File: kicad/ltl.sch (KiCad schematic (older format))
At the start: 17 parts, among them J1 CONN_01X03, J2 BARREL_JACK, SW1 SW_DIP_x02, SW2 SW_DIP_x02, U1 ESP-12E, U2 DS18B20

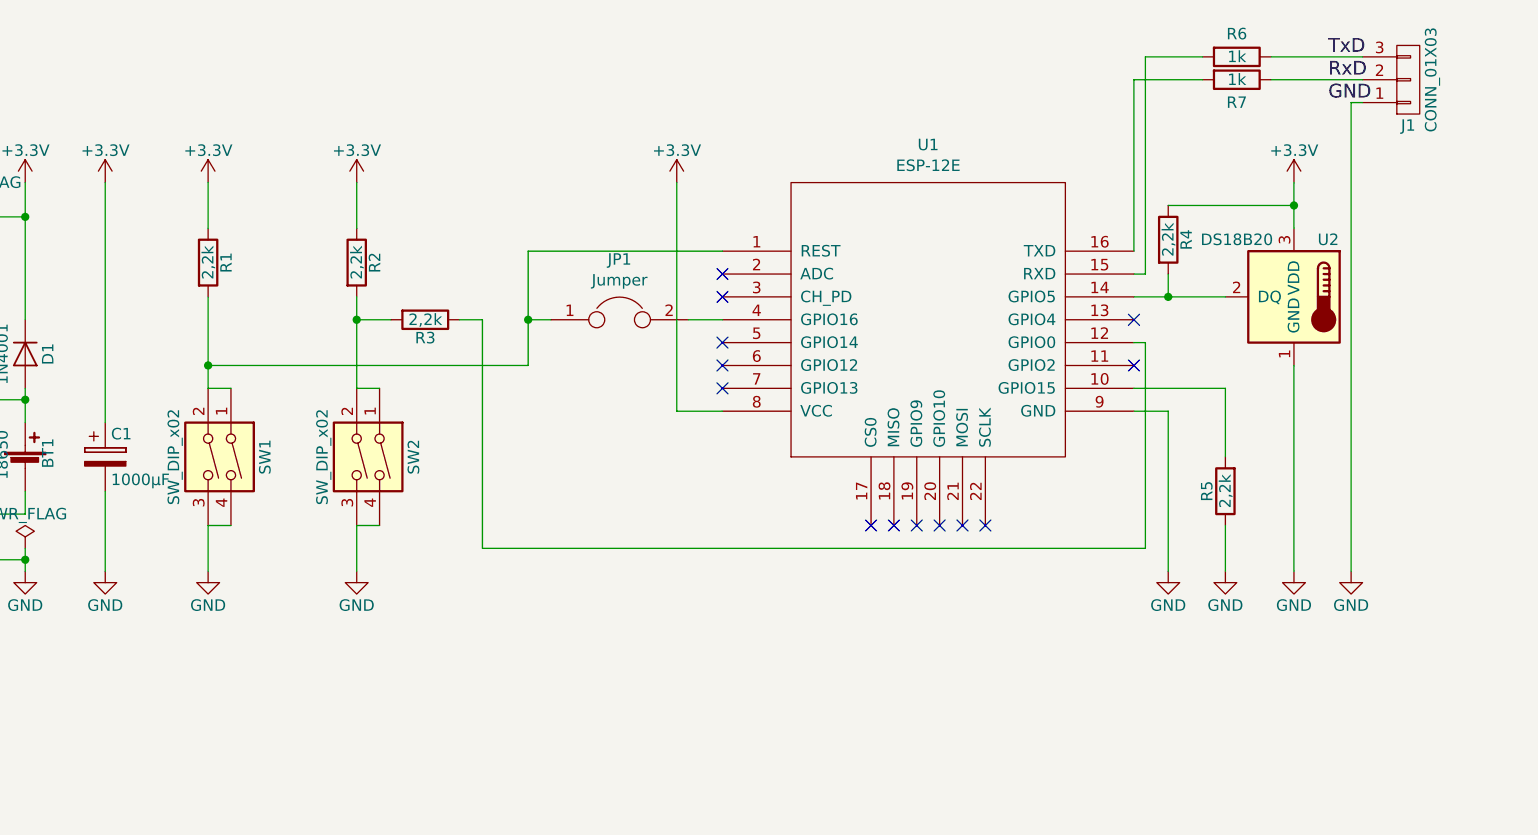
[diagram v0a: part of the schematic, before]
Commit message: Zweite Revision der Leiterplatte, mehrere Fehler beseitigt: - Schalter Symbol und Footprint haben nicht übereingestimmt (Nummerierung), dadurch nur mit Schwierigkeiten einsetzbar (3 Leiterbahnen müssen entfernt werden) - Beim ESP8266 muss der Chip Enable Pin auf High gesetzt werden - Beim UART RxD und TxD vertauscht - Befestigungslöcher etwas vergrößert (von 2mm auf 2,7mm)
Desweiteren noch ein aktualisiertes 3D Image der Leiterplatte hinzugefügt.

Anonsten ist der erste Prototyp funktionsfähig :)
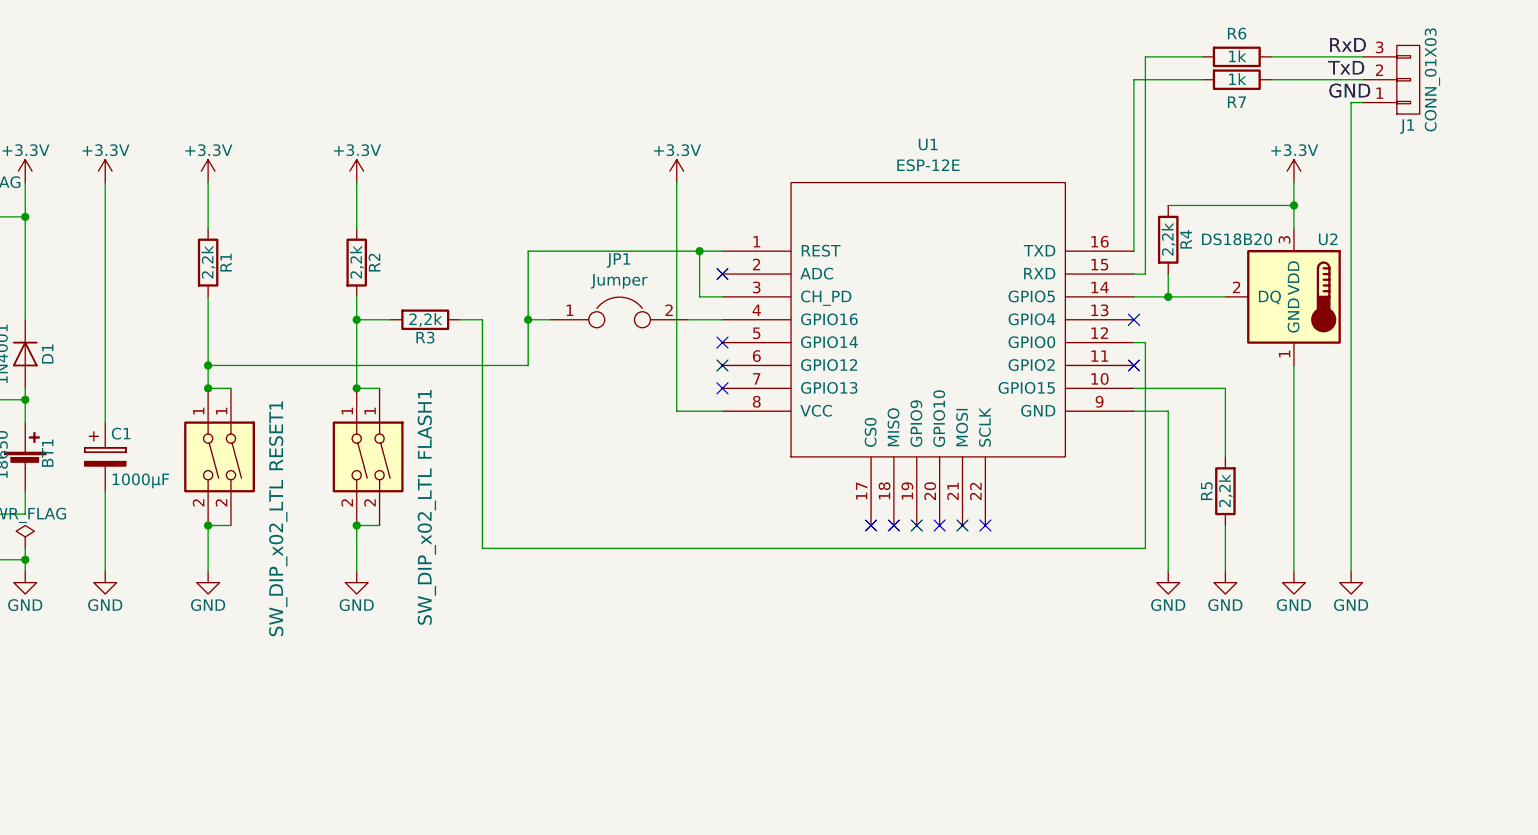
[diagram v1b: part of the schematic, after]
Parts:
- removed SW1, SW2: SW_DIP_x02, Button_Switch_THT:SW_PUSH_6mm_H5mm, symbol ltl-rescue:SW_DIP_x02
- added FLASH1, RESET1: SW_DIP_x02_LTL, Button_Switch_THT:SW_PUSH_6mm, symbol LTL:SW_DIP_x02_LTL
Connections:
- net GND: now also FLASH1.2, RESET1.2
- net RxD: now also J1.3 (P3), R6.1; no longer J1.2 (P2), R7.1
- net TxD: now also J1.2 (P2), R7.1; no longer J1.3 (P3), R6.1
- net at JP1.1, R1.2, U1.1 (REST): now also U1.3 (CH_PD), RESET1.1
- net at R2.2, R3.2: now also FLASH1.1
- no-connect marks 14 -> 13
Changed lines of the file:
@@
-	0    1    1    0
-$EndComp
-$Comp
-L ltl-rescue:SW_DIP_x02 SW1
-U 1 1 59EEEDEE
-P 2600 3400
-F 0 "SW1" H 2600 3650 50  0000 C CNN
-F 1 "SW_DIP_x02" H 2600 3250 50  0000 C CNN
-F 2 "Button_Switch_THT:SW_PUSH_6mm_H5mm" H 2600 3400 50  0001 C CNN
-F 3 "" H 2600 3400 50  0001 C CNN
-	1    2600 3400
-	0    1    1    0
-$EndComp
-$Comp
-L ltl-rescue:SW_DIP_x02 SW2
-U 1 1 59EEEE4D
-P 3250 3400
-F 0 "SW2" H 3250 3650 50  0000 C CNN
-F 1 "SW_DIP_x02" H 3250 3250 50  0000 C CNN
-F 2 "Button_Switch_THT:SW_PUSH_6mm_H5mm" H 3250 3400 50  0001 C CNN
-F 3 "" H 3250 3400 50  0001 C CNN
-	1    3250 3400
 	0    1    1    0
 $EndComp
@@
 Connection ~ 3250 2800
 Wire Wire Line
-	4850 2500 4000 2500
+	4850 2500 4750 2500
 Wire Wire Line
 	4000 3000 2600 3000
@@
 Wire Wire Line
 	7600 1850 7600 3900
+Text Label 7500 1750 0    60   ~ 0
+TxD
 Text Label 7500 1650 0    60   ~ 0
-TxD
-Text Label 7500 1750 0    60   ~ 0
 RxD
 Text Label 7500 1850 0    60   ~ 0
@@
 	1800 3650 1800 3550
 NoConn ~ 4850 2600
-NoConn ~ 4850 2700
 NoConn ~ 4850 2900
 NoConn ~ 4850 3000
@@
 	1    0    0    -1
 $EndComp
+Wire Wire Line
+	4850 2700 4750 2700
+Wire Wire Line
+	4750 2700 4750 2500
+Connection ~ 4750 2500
+Wire Wire Line
+	4750 2500 4000 2500
+$Comp
+L LTL:SW_DIP_x02_LTL RESET1
+U 1 1 5E7676F5
+P 2650 3400
+F 0 "RESET1" H 2400 3650 60  0000 L CNN
+F 1 "SW_DIP_x02_LTL" H 2750 3650 60  0000 L CNN
+F 2 "Button_Switch_THT:SW_PUSH_6mm" H 2650 3400 60  0001 C CNN
+F 3 "" H 2650 3400 60  0001 C CNN
+	1    2650 3400
+	0    1    1    0
+$EndComp
+Connection ~ 2600 3100
+Connection ~ 2600 3700
+$Comp
+L LTL:SW_DIP_x02_LTL FLASH1
+U 1 1 5E769C54
+P 3300 3400
+F 0 "FLASH1" H 3000 3650 60  0000 L CNN
+F 1 "SW_DIP_x02_LTL" H 3350 3650 60  0000 L CNN
+F 2 "Button_Switch_THT:SW_PUSH_6mm" H 3300 3400 60  0001 C CNN
+F 3 "" H 3300 3400 60  0001 C CNN
+	1    3300 3400
+	0    1    1    0
+$EndComp
+Connection ~ 3250 3100
+Connection ~ 3250 3700
 $EndSCHEMATC
